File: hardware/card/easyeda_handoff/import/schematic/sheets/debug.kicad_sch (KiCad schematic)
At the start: 2 parts, among them U5 DRV2605LDGS

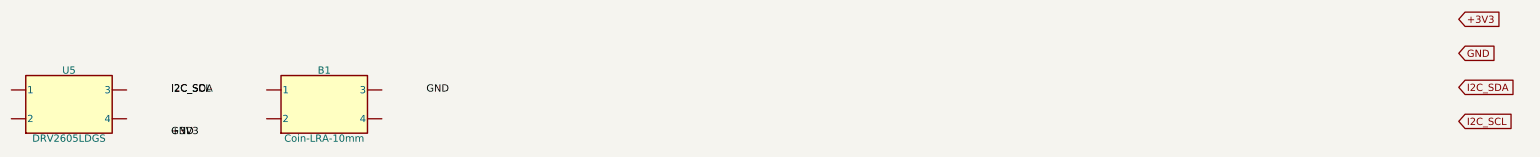
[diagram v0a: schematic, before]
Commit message: Add handheld card EasyEDA handoff
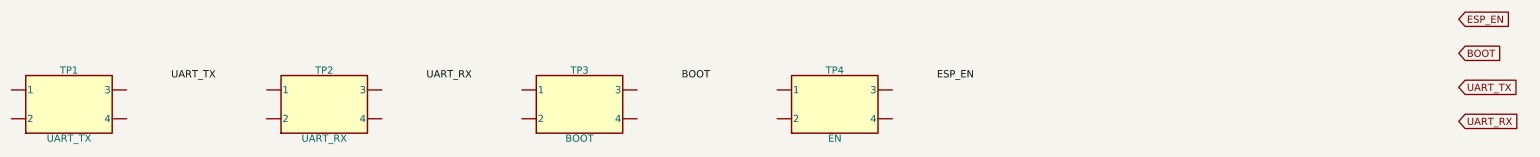
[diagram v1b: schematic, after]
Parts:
- removed B1: Coin-LRA-10mm, TBD, symbol PSCard:Block2
- removed U5: DRV2605LDGS, VSSOP-10-DGS-3x4.9, symbol PSCard:Block2
- added TP1: UART_TX, TestPoint, symbol PSCard:Block2
- added TP2: UART_RX, TestPoint, symbol PSCard:Block2
- added TP3: BOOT, TestPoint, symbol PSCard:Block2
- added TP4: EN, TestPoint, symbol PSCard:Block2
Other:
- title: PuzzleScript Card — haptic -> PuzzleScript Card — debug
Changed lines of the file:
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@@
   (paper "A4")
   (title_block
-    (title "PuzzleScript Card — haptic")
+    (title "PuzzleScript Card — debug")
     (date "2026-07-09")
     (rev "spin1")
@@
   (symbol (lib_id "PSCard:Block2") (at 35 35 0) (unit 1)
     (exclude_from_sim no) (in_bom yes) (on_board yes) (dnp no) (fields_autoplaced)
-    (property "Reference" "U5" (at 35 29 0)
+    (property "Reference" "TP1" (at 35 29 0)
       (effects (font (size 1.27 1.27))))
-    (property "Value" "DRV2605LDGS" (at 35 41 0)
+    (property "Value" "UART_TX" (at 35 41 0)
       (effects (font (size 1.27 1.27))))
-    (property "Footprint" "VSSOP-10-DGS-3x4.9" (at 35 35 0)
+    (property "Footprint" "TestPoint" (at 35 35 0)
       (effects (font (size 1.27 1.27)) hide))
     (property "Datasheet" "~" (at 35 35 0)
       (effects (font (size 1.27 1.27)) hide))
-    (instances (project "card" (path "/card/sheets/haptic" (reference "U5") (unit 1))))
+    (instances (project "card" (path "/card/sheets/debug" (reference "TP1") (unit 1))))
   )
-  (label "+3V3" (at 53 40 0) (fields_autoplaced)
-    (effects (font (size 1.27 1.27)) (justify left)))
-  (label "GND" (at 53 40 0) (fields_autoplaced)
-    (effects (font (size 1.27 1.27)) (justify left)))
-  (label "I2C_SDA" (at 53 32.5 0) (fields_autoplaced)
-    (effects (font (size 1.27 1.27)) (justify left)))
-  (label "I2C_SCL" (at 53 32.5 0) (fields_autoplaced)
+  (label "UART_TX" (at 53 30 0) (fields_autoplaced)
     (effects (font (size 1.27 1.27)) (justify left)))
   (symbol (lib_id "PSCard:Block2") (at 80 35 0) (unit 1)
     (exclude_from_sim no) (in_bom yes) (on_board yes) (dnp no) (fields_autoplaced)
-    (property "Reference" "B1" (at 80 29 0)
+    (property "Reference" "TP2" (at 80 29 0)
       (effects (font (size 1.27 1.27))))
-    (property "Value" "Coin-LRA-10mm" (at 80 41 0)
+    (property "Value" "UART_RX" (at 80 41 0)
       (effects (font (size 1.27 1.27))))
-    (property "Footprint" "TBD" (at 80 35 0)
+    (property "Footprint" "TestPoint" (at 80 35 0)
       (effects (font (size 1.27 1.27)) hide))
     (property "Datasheet" "~" (at 80 35 0)
       (effects (font (size 1.27 1.27)) hide))
-    (property "Gate" "GATE-LRA-MOUNT" (at 80 35 0)
+    (instances (project "card" (path "/card/sheets/debug" (reference "TP2") (unit 1))))
+  )
+  (label "UART_RX" (at 98 30 0) (fields_autoplaced)
+    (effects (font (size 1.27 1.27)) (justify left)))
+  (symbol (lib_id "PSCard:Block2") (at 125 35 0) (unit 1)
+    (exclude_from_sim no) (in_bom yes) (on_board yes) (dnp no) (fields_autoplaced)
+    (property "Reference" "TP3" (at 125 29 0)
+      (effects (font (size 1.27 1.27))))
+    (property "Value" "BOOT" (at 125 41 0)
+      (effects (font (size 1.27 1.27))))
+    (property "Footprint" "TestPoint" (at 125 35 0)
       (effects (font (size 1.27 1.27)) hide))
-    (instances (project "card" (path "/card/sheets/haptic" (reference "B1") (unit 1))))
+    (property "Datasheet" "~" (at 125 35 0)
+      (effects (font (size 1.27 1.27)) hide))
+    (instances (project "card" (path "/card/sheets/debug" (reference "TP3") (unit 1))))
   )
-  (label "GND" (at 98 32.5 0) (fields_autoplaced)
+  (label "BOOT" (at 143 30 0) (fields_autoplaced)
     (effects (font (size 1.27 1.27)) (justify left)))
-  (global_label "+3V3" (shape input) (at 280 20 0) (fields_autoplaced)
+  (symbol (lib_id "PSCard:Block2") (at 170 35 0) (unit 1)
+    (exclude_from_sim no) (in_bom yes) (on_board yes) (dnp no) (fields_autoplaced)
+    (property "Reference" "TP4" (at 170 29 0)
+      (effects (font (size 1.27 1.27))))
+    (property "Value" "EN" (at 170 41 0)
+      (effects (font (size 1.27 1.27))))
+    (property "Footprint" "TestPoint" (at 170 35 0)
+      (effects (font (size 1.27 1.27)) hide))
+    (property "Datasheet" "~" (at 170 35 0)
+      (effects (font (size 1.27 1.27)) hide))
+    (instances (project "card" (path "/card/sheets/debug" (reference "TP4") (unit 1))))
+  )
+  (label "ESP_EN" (at 188 30 0) (fields_autoplaced)
+    (effects (font (size 1.27 1.27)) (justify left)))
+  (global_label "ESP_EN" (shape input) (at 280 20 0) (fields_autoplaced)
     (effects (font (size 1.27 1.27)) (justify left))
     (property "Intersheetrefs" "${INTERSHEET_REFS}" (at 280 20 0)
       (effects (font (size 1.27 1.27)) hide))
   )
-  (global_label "GND" (shape input) (at 280 26 0) (fields_autoplaced)
+  (global_label "BOOT" (shape input) (at 280 26 0) (fields_autoplaced)
     (effects (font (size 1.27 1.27)) (justify left))
     (property "Intersheetrefs" "${INTERSHEET_REFS}" (at 280 26 0)
       (effects (font (size 1.27 1.27)) hide))
   )
-  (global_label "I2C_SDA" (shape input) (at 280 32 0) (fields_autoplaced)
+  (global_label "UART_TX" (shape input) (at 280 32 0) (fields_autoplaced)
     (effects (font (size 1.27 1.27)) (justify left))
     (property "Intersheetrefs" "${INTERSHEET_REFS}" (at 280 32 0)
       (effects (font (size 1.27 1.27)) hide))
   )
-  (global_label "I2C_SCL" (shape input) (at 280 38 0) (fields_autoplaced)
+  (global_label "UART_RX" (shape input) (at 280 38 0) (fields_autoplaced)
     (effects (font (size 1.27 1.27)) (justify left))
     (property "Intersheetrefs" "${INTERSHEET_REFS}" (at 280 38 0)

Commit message: puzzlescript hardware case
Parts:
- TP1, TP2, TP3, TP4: footprint TestPoint -> TestPoint_Pad_D1.5mm
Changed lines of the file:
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@@
     (property "Value" "UART_TX" (at 35 41 0)
       (effects (font (size 1.27 1.27))))
-    (property "Footprint" "TestPoint" (at 35 35 0)
+    (property "Footprint" "TestPoint_Pad_D1.5mm" (at 35 35 0)
       (effects (font (size 1.27 1.27)) hide))
     (property "Datasheet" "~" (at 35 35 0)
@@
     (property "Value" "UART_RX" (at 80 41 0)
       (effects (font (size 1.27 1.27))))
-    (property "Footprint" "TestPoint" (at 80 35 0)
+    (property "Footprint" "TestPoint_Pad_D1.5mm" (at 80 35 0)
       (effects (font (size 1.27 1.27)) hide))
     (property "Datasheet" "~" (at 80 35 0)
@@
     (property "Value" "BOOT" (at 125 41 0)
       (effects (font (size 1.27 1.27))))
-    (property "Footprint" "TestPoint" (at 125 35 0)
+    (property "Footprint" "TestPoint_Pad_D1.5mm" (at 125 35 0)
       (effects (font (size 1.27 1.27)) hide))
     (property "Datasheet" "~" (at 125 35 0)
@@
     (property "Value" "EN" (at 170 41 0)
       (effects (font (size 1.27 1.27))))
-    (property "Footprint" "TestPoint" (at 170 35 0)
+    (property "Footprint" "TestPoint_Pad_D1.5mm" (at 170 35 0)
       (effects (font (size 1.27 1.27)) hide))
     (property "Datasheet" "~" (at 170 35 0)
